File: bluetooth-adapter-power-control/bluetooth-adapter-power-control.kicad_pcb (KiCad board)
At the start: 2 copper layers, 14 parts, among them J1 UPDI, J2 HDR, Q1 NMOS, U1 ATtiny202-SSNR

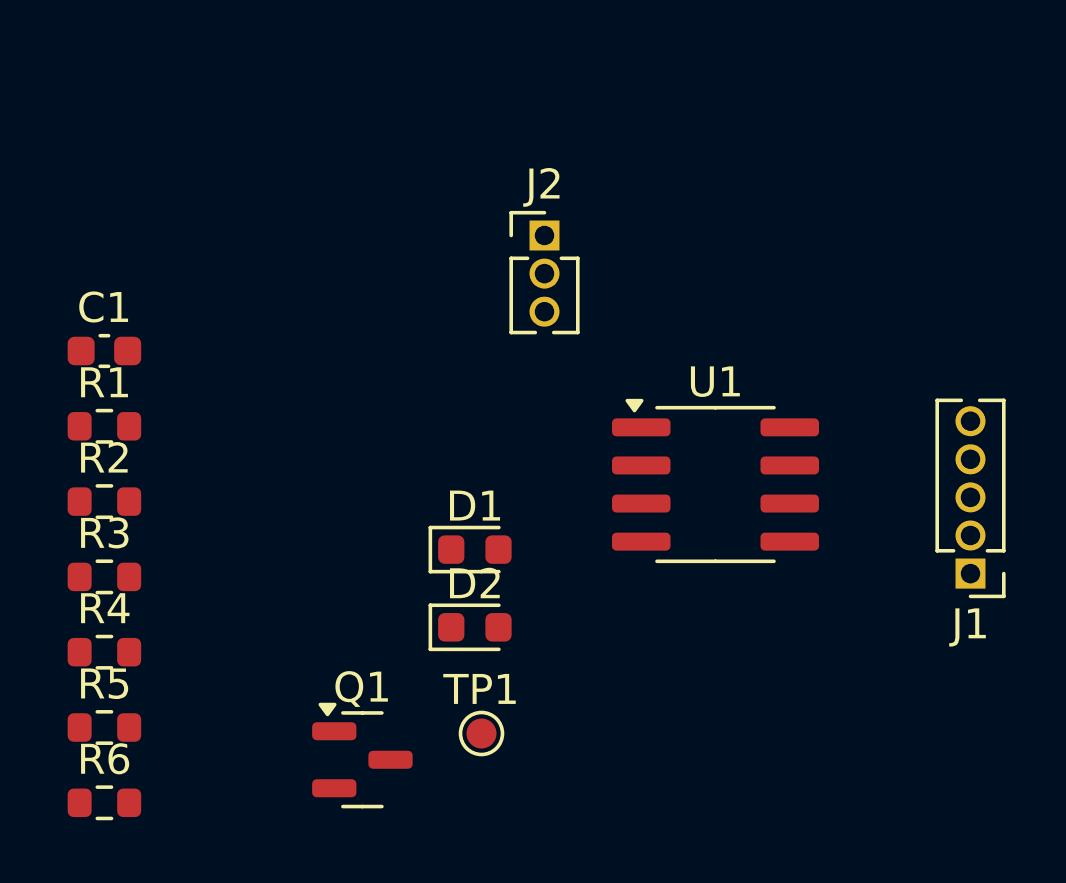
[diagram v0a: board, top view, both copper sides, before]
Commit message: bluetooth-adapter-power-control: change 5 pin header to 7 to include button short pins
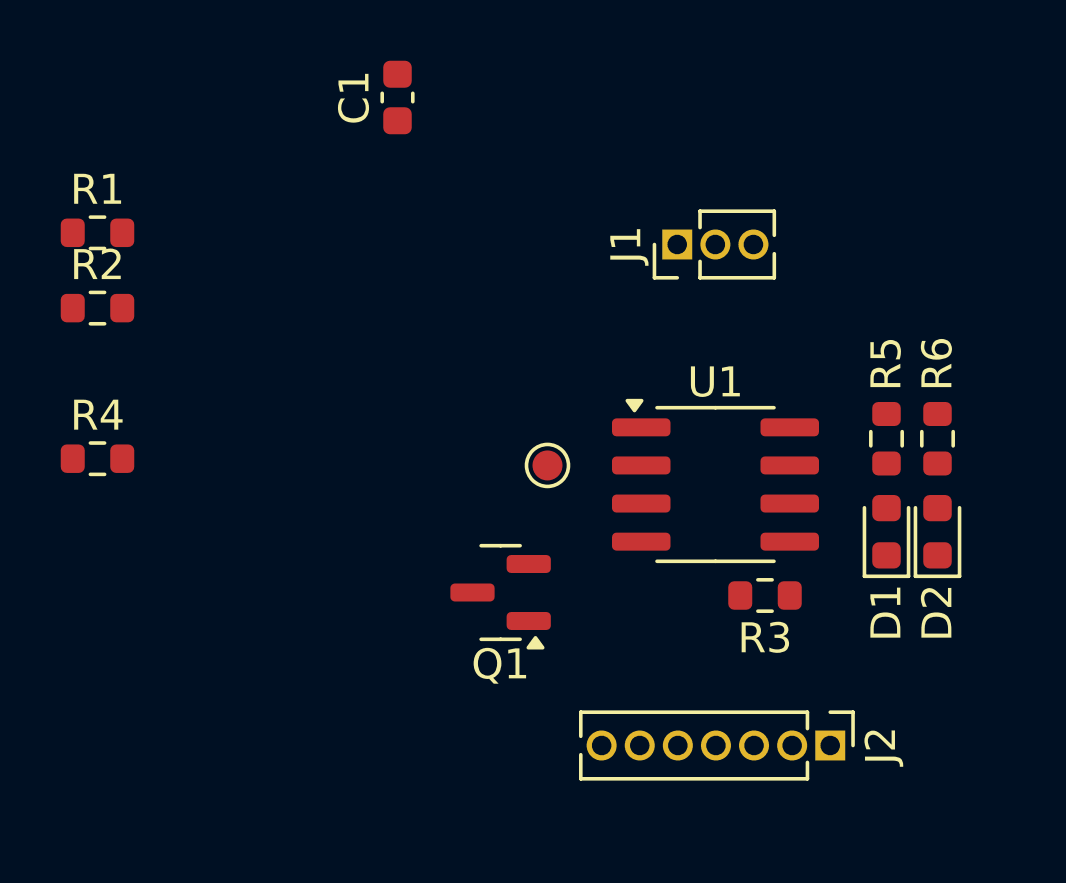
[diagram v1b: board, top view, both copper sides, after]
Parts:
- J1: footprint Connector_PinHeader_1.27mm:PinHeader_1x05_P1.27mm_Vertical -> Connector_PinHeader_1.27mm:PinHeader_1x03_P1.27mm_Vertical
- J2: value HDR -> Conn_01x07_Socket; footprint Connector_PinHeader_1.27mm:PinHeader_1x03_P1.27mm_Vertical -> Connector_PinHeader_1.27mm:PinHeader_1x07_P1.27mm_Vertical
- moved R6 30.3 mm to (151.9, 65.3), turned to -90 degrees
- moved R5 27.8 mm to (150.2, 65.3), turned to -90 degrees
- moved R3 22.0 mm to (146.2, 70.5), turned to 180 degrees
- moved J2 19.5 mm to (148.3, 75.5), turned to -90 degrees
- moved D2 15.7 mm to (151.9, 68.4), turned to 90 degrees
- moved J1 14.7 mm to (143.2, 58.8), turned to 90 degrees
- moved D1 13.7 mm to (150.2, 68.4), turned to 90 degrees
- moved C1 12.9 mm to (133.9, 53.9), turned to 90 degrees
- moved TP1 9.20 mm to (138.9, 66.2)
- moved Q1 7.23 mm to (137.3, 70.4), turned to 180 degrees
- moved R1 6.45 mm to (123.9, 58.4)
- moved R2 6.45 mm to (123.9, 60.9)
- moved R4 6.45 mm to (123.9, 65.9)
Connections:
- J2 pad 3: CAR_ON -> IGNITION_IN

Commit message: bluetooth-adapter-power-control: initial PCB layout (no routing)
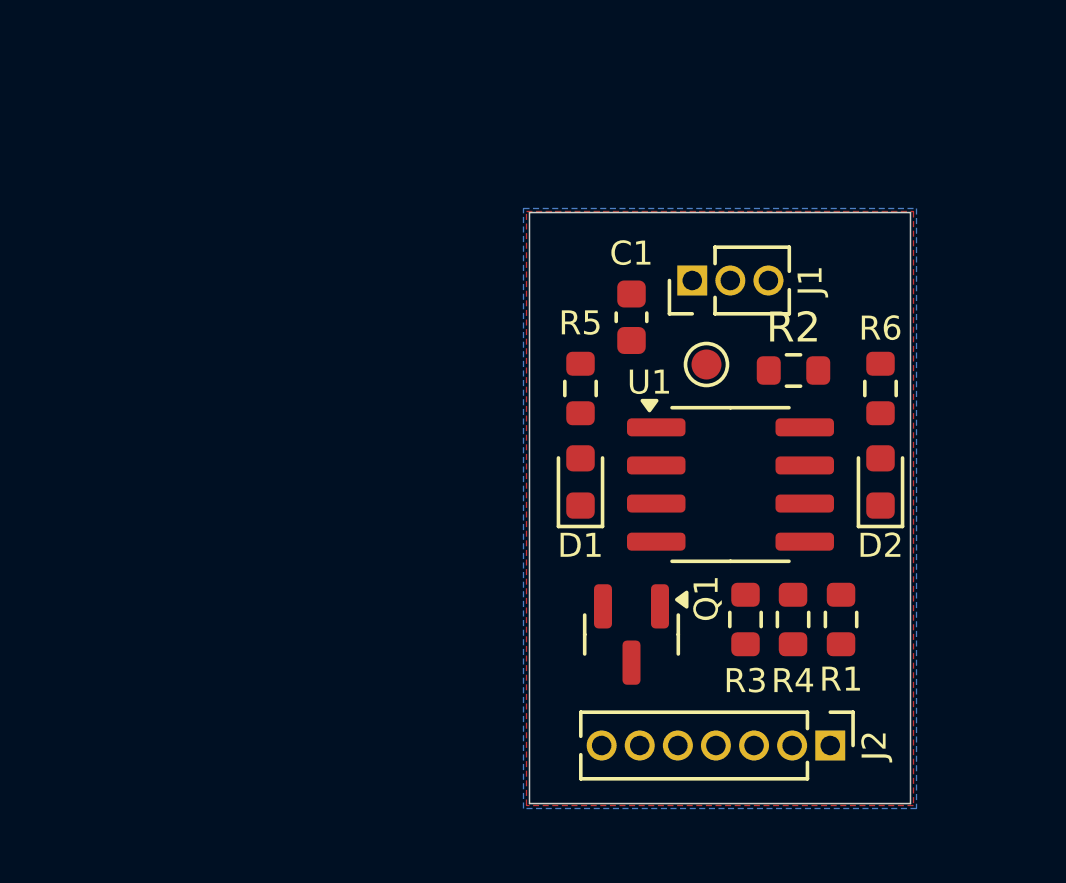
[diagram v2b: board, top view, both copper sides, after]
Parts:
- moved R1 27.9 mm to (148.7, 71.3), turned to 90 degrees
- moved R4 23.8 mm to (147.1, 71.3), turned to -90 degrees
- moved R2 23.3 mm to (147.1, 63.0)
- moved C1 10.7 mm to (141.7, 61.2)
- moved R5 10.3 mm to (140.0, 63.6)
- moved D1 10.3 mm to (140.0, 66.7)
- moved TP1 6.28 mm to (144.2, 62.8)
- moved Q1 4.58 mm to (141.7, 71.8), turned to -90 degrees
- moved R6 2.53 mm to (150.0, 63.6)
- moved D2 2.52 mm to (150.0, 66.7)
- moved J1 1.30 mm to (143.7, 60.0)
- moved R3 1.03 mm to (145.5, 71.3), turned to 90 degrees
- moved U1 0.50 mm to (145.0, 66.8)
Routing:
- added copper zone on F.Cu, net +5V
- added copper zone on B.Cu, net GND
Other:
- board outline added: 12.7 x 19.7 mm

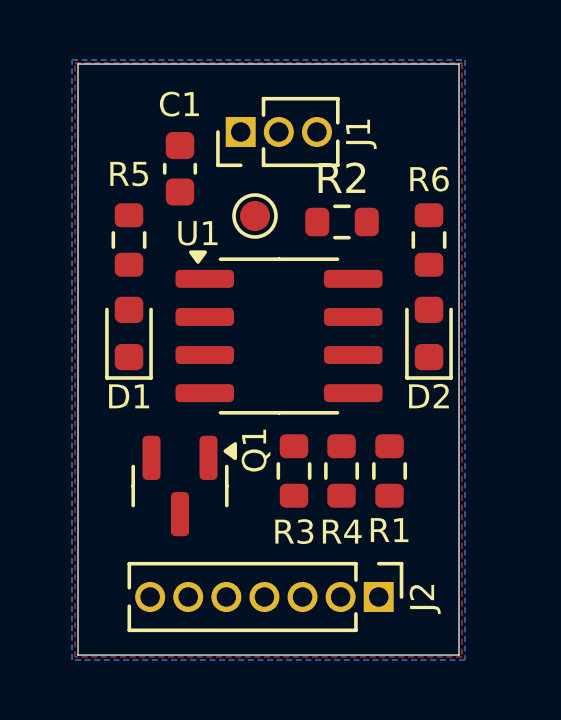
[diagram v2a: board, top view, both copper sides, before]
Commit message: bluetooth-adapter-power-control: Finish PCB routing
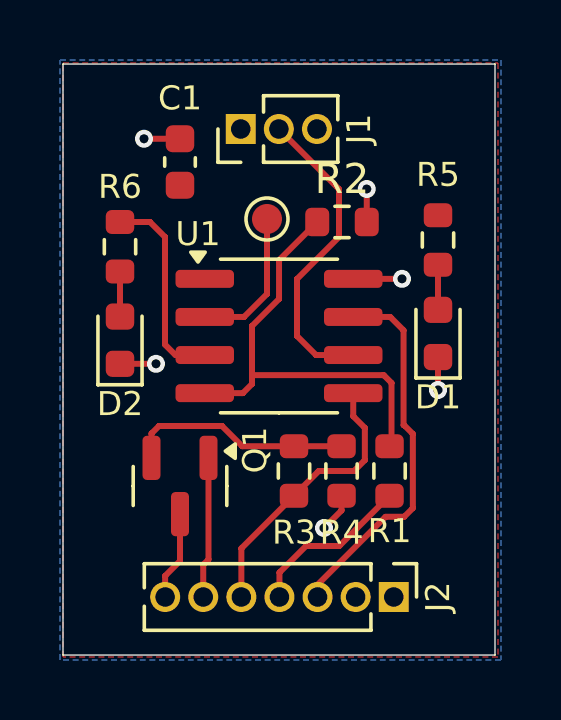
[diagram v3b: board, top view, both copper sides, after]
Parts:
- moved D2 10.3 mm to (139.7, 66.9)
- moved R6 10.3 mm to (139.7, 63.8)
- moved D1 10.3 mm to (150.3, 66.7)
- moved R5 10.3 mm to (150.3, 63.6)
- moved J2 0.50 mm to (148.8, 75.5)
- moved TP1 0.41 mm to (144.6, 62.9)
- moved C1 0.23 mm to (141.7, 61.0)
- moved J1 0.10 mm to (143.7, 59.9)
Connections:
- J2 pad 3: IGNITION_IN -> BT_LED_IN
- J2 pad 4: BTN_SHORT -> IGNITION_IN
- J2 pad 5: BT_LED_IN -> BTN_SHORT
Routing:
- net CAR_ON: track 0.00 -> 14.9 mm
- net BT_LED_IN: track 0.00 -> 12.6 mm
- net UPDI: track 0.00 -> 10.4 mm
- net BTN_SHORT: track 0.00 -> 9.35 mm
- net GND: track 0.00 -> 7.54 mm, vias 0 -> 6
- net Net-(Q1-G): track 0.00 -> 7.53 mm
- net Net-(U1-PA7): track 0.00 -> 6.76 mm
- net IGNITION_IN: track 0.00 -> 5.55 mm
- net Net-(U1-PA6): track 0.00 -> 4.89 mm
- net BTN1: track 0.00 -> 4.71 mm
- net BTN2: track 0.00 -> 2.97 mm
- net Net-(D2-A): track 0.00 -> 1.50 mm
- net Net-(D1-A): track 0.00 -> 1.50 mm
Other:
- board size 12.7 x 19.7 mm -> 14.4 x 19.7 mm

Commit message: bluetooth-adapter-power-control: Change ignition voltage resistor divider to use a zener diode
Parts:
- removed R2: 7.5k, Resistor_SMD:R_0603_1608Metric
- added D3: 5.1V, Diode_SMD:D_SOD-523, F.Cu at (147.1, 63.0)

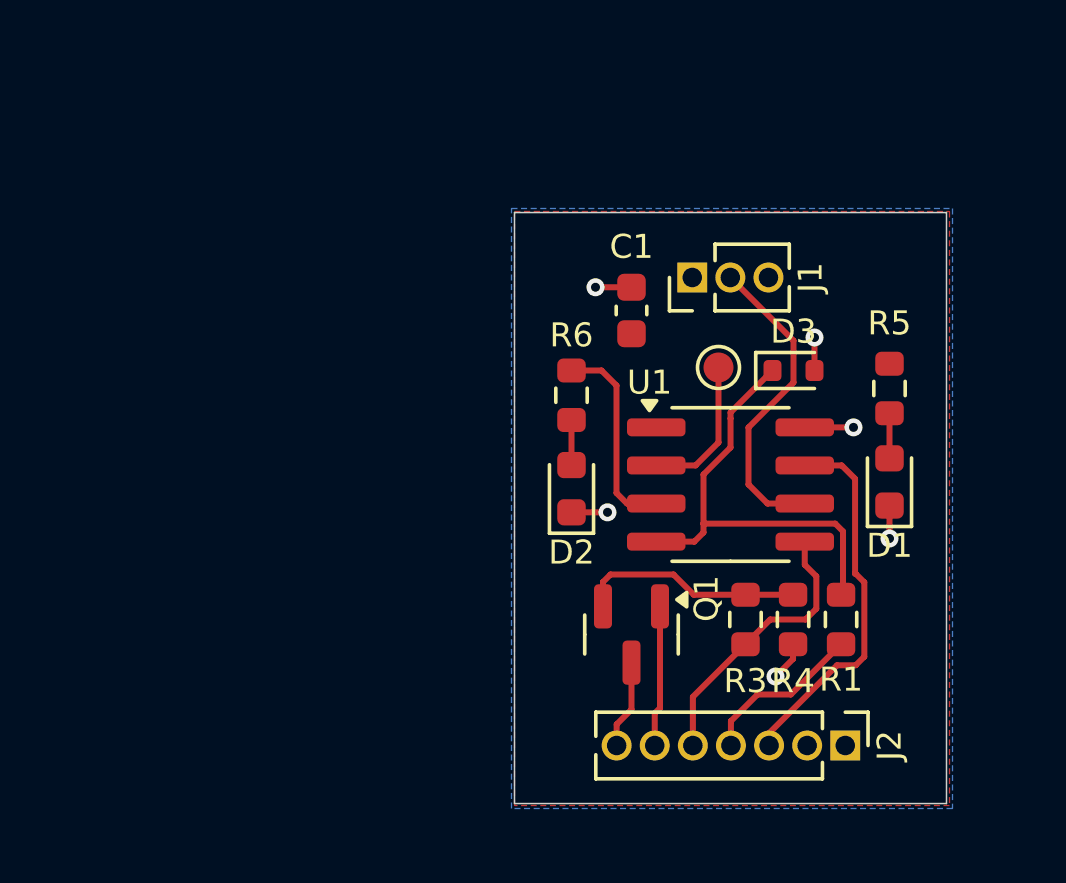
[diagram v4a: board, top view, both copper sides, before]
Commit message: bluetooth-adapter-power-control: Add pin labels and 1mm mounting holes
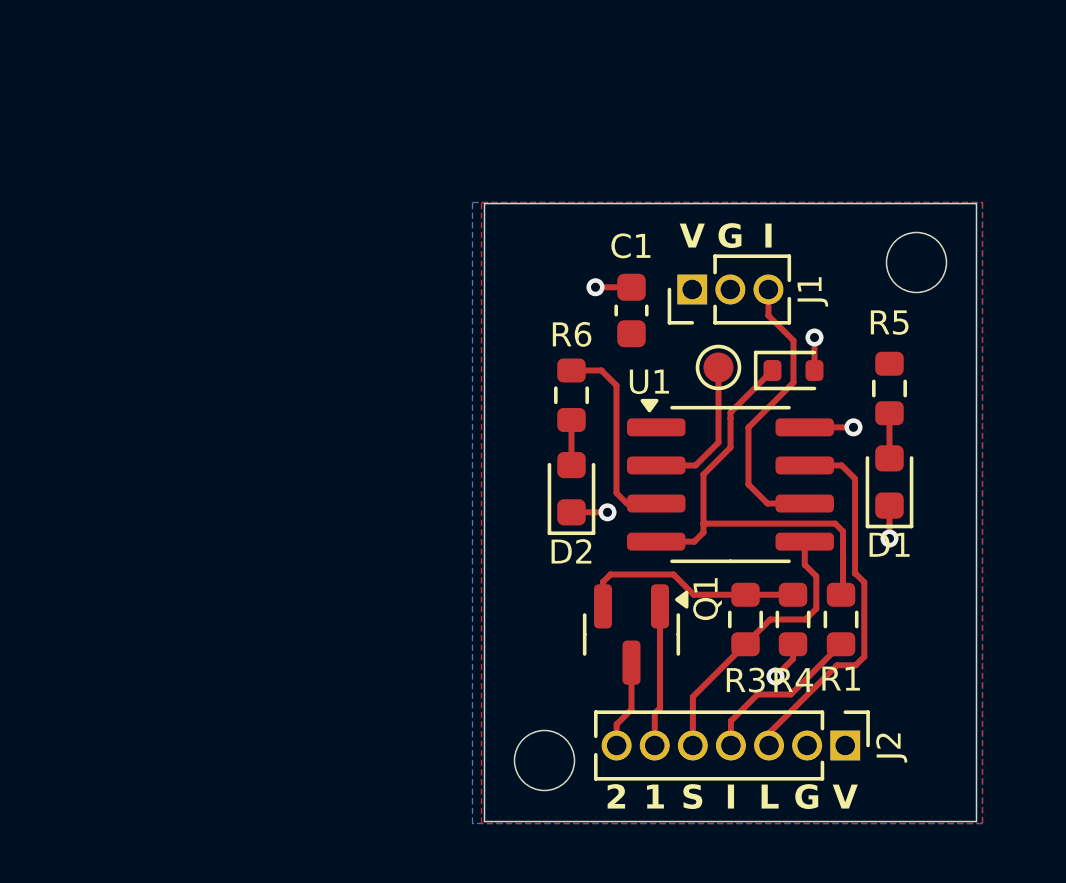
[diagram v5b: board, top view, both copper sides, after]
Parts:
- moved J1 0.40 mm to (143.7, 60.3)
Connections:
- J1 pad 2: UPDI -> GND
- J1 pad 3: GND -> UPDI
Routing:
- net UPDI: track 10.5 -> 9.61 mm
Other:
- board size 14.4 x 19.7 mm -> 16.4 x 20.6 mm
- board text added: "1"
- board text added: "2"
- board text added: "G"
- board text added: "I"
- board text added: "L"
- board text added: "S"
- board text added: "V"
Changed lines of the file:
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@@
 			(at 0 -1.3 0)
 			(layer "F.SilkS")
+			(hide yes)
 			(effects
 				(font
@@
 	(footprint "Connector_PinHeader_1.27mm:PinHeader_1x03_P1.27mm_Vertical"
 		(layer "F.Cu")
-		(at 143.725 59.9 90)
+		(at 143.725 60.3 90)
 		(descr "Through hole straight pin header, 1x03, 1.27mm pitch, single row")
 		(tags "Through hole pin header THT 1x03 1.27mm single row")
@@
 			(layers "*.Cu" "*.Mask")
 			(remove_unused_layers no)
-			(net 5 "UPDI")
+			(net 2 "GND")
 			(pinfunction "Pin_2")
 			(pintype "passive")
@@
 			(layers "*.Cu" "*.Mask")
 			(remove_unused_layers no)
-			(net 2 "GND")
+			(net 5 "UPDI")
 			(pinfunction "Pin_3")
 			(pintype "passive")
@@
 	)
 	(gr_rect
-		(start 137.8 57.735)
-		(end 152.2 77.435)
+		(start 136.8 57.435)
+		(end 153.2 78.035)
 		(stroke
 			(width 0.05)
@@
 		(fill no)
 		(layer "Edge.Cuts")
+	)
+	(gr_circle
+		(center 151.2 59.4)
+		(end 151.8 60.2)
+		(stroke
+			(width 0.05)
+			(type default)
+		)
+		(fill no)
+		(layer "Edge.Cuts")
+	)
+	(gr_circle
+		(center 138.8 76)
+		(end 139.4 76.8)
+		(stroke
+			(width 0.05)
+			(type default)
+		)
+		(fill no)
+		(layer "Edge.Cuts")
+	)
+	(gr_text "I"
+		(at 145.015 77.7 0)
+		(layer "F.SilkS")
+		(effects
+			(font
+				(size 0.8 0.8)
+				(thickness 0.16)
+				(bold yes)
+			)
+			(justify bottom)
+		)
+	)
+	(gr_text "I"
+		(at 146.265 59 0)
+		(layer "F.SilkS")
+		(effects
+			(font
+				(size 0.8 0.8)
+				(thickness 0.16)
+				(bold yes)
+			)
+			(justify bottom)
+		)
+	)
+	(gr_text "G"
+		(at 147.555 77.7 0)
+		(layer "F.SilkS")
+		(effects
+			(font
+				(size 0.8 0.8)
+				(thickness 0.16)
+				(bold yes)
+			)
+			(justify bottom)
+		)
+	)
+	(gr_text "V"
+		(at 143.725 59 0)
+		(layer "F.SilkS")
+		(effects
+			(font
+				(size 0.8 0.8)
+				(thickness 0.16)
+				(bold yes)
+			)
+			(justify bottom)
+		)
+	)
+	(gr_text "L"
+		(at 146.285 77.7 0)
+		(layer "F.SilkS")
+		(effects
+			(font
+				(size 0.8 0.8)
+				(thickness 0.16)
+				(bold yes)
+			)
+			(justify bottom)
+		)
+	)
+	(gr_text "2"
+		(at 141.2 77.7 0)
+		(layer "F.SilkS")
+		(effects
+			(font
+				(size 0.8 0.8)
+				(thickness 0.16)
+				(bold yes)
+			)
+			(justify bottom)
+		)
+	)
+	(gr_text "G"
+		(at 144.995 59 0)
+		(layer "F.SilkS")
+		(effects
+			(font
+				(size 0.8 0.8)
+				(thickness 0.16)
+				(bold yes)
+			)
+			(justify bottom)
+		)
+	)
+	(gr_text "V"
+		(at 148.825 77.7 0)
+		(layer "F.SilkS")
+		(effects
+			(font
+				(size 0.8 0.8)
+				(thickness 0.16)
+				(bold yes)
+			)
+			(justify bottom)
+		)
+	)
+	(gr_text "1"
+		(at 142.475 77.7 0)
+		(layer "F.SilkS")
+		(effects
+			(font
+				(size 0.8 0.8)
+				(thickness 0.16)
+				(bold yes)
+			)
+			(justify bottom)
+		)
+	)
+	(gr_text "S"
+		(at 143.745 77.7 0)
+		(layer "F.SilkS")
+		(effects
+			(font
+				(size 0.8 0.8)
+				(thickness 0.16)
+				(bold yes)
+			)
+			(justify bottom)
+		)
 	)
 	(segment
@@
 	)
 	(segment
-		(start 144.995 59.9)
-		(end 147.1 62.005)
+		(start 146.265 61.17)
+		(end 146.265 60.3)
 		(width 0.2)
 		(layer "F.Cu")
@@
 		(start 145.6 64.9)
 		(end 145.6 66.8)
+		(width 0.2)
+		(layer "F.Cu")
+		(net 5)
+	)
+	(segment
+		(start 147.1 62.005)
+		(end 146.265 61.17)
 		(width 0.2)
 		(layer "F.Cu")
@@
 		(polygon
 			(pts
-				(xy 137.8 57.7) (xy 152.3 57.7) (xy 152.3 77.5) (xy 137.8 77.5)
+				(xy 136.7 57.4) (xy 153.4 57.4) (xy 153.4 78.1) (xy 136.7 78.1)
 			)
 		)
@@
 		(polygon
 			(pts
-				(xy 137.7 57.6) (xy 152.4 57.6) (xy 152.4 77.6) (xy 137.7 77.6)
-			)
-		)
+				(xy 136.4 57.4) (xy 153.4 57.4) (xy 153.4 78.1) (xy 136.4 78.1)
+			)
+		)
